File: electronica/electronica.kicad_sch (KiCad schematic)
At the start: 19 parts, among them J1 Arduino_Power, J10 Pump_4, J2 ESP12_Power, J3 Arduino_Serial, J4 DC 5v, J5 ESP12_Serial, J6 Arduino_D8_D11, J7 Pump_1, J8 Pump_2, J9 Pump_3, U1 ULN2003

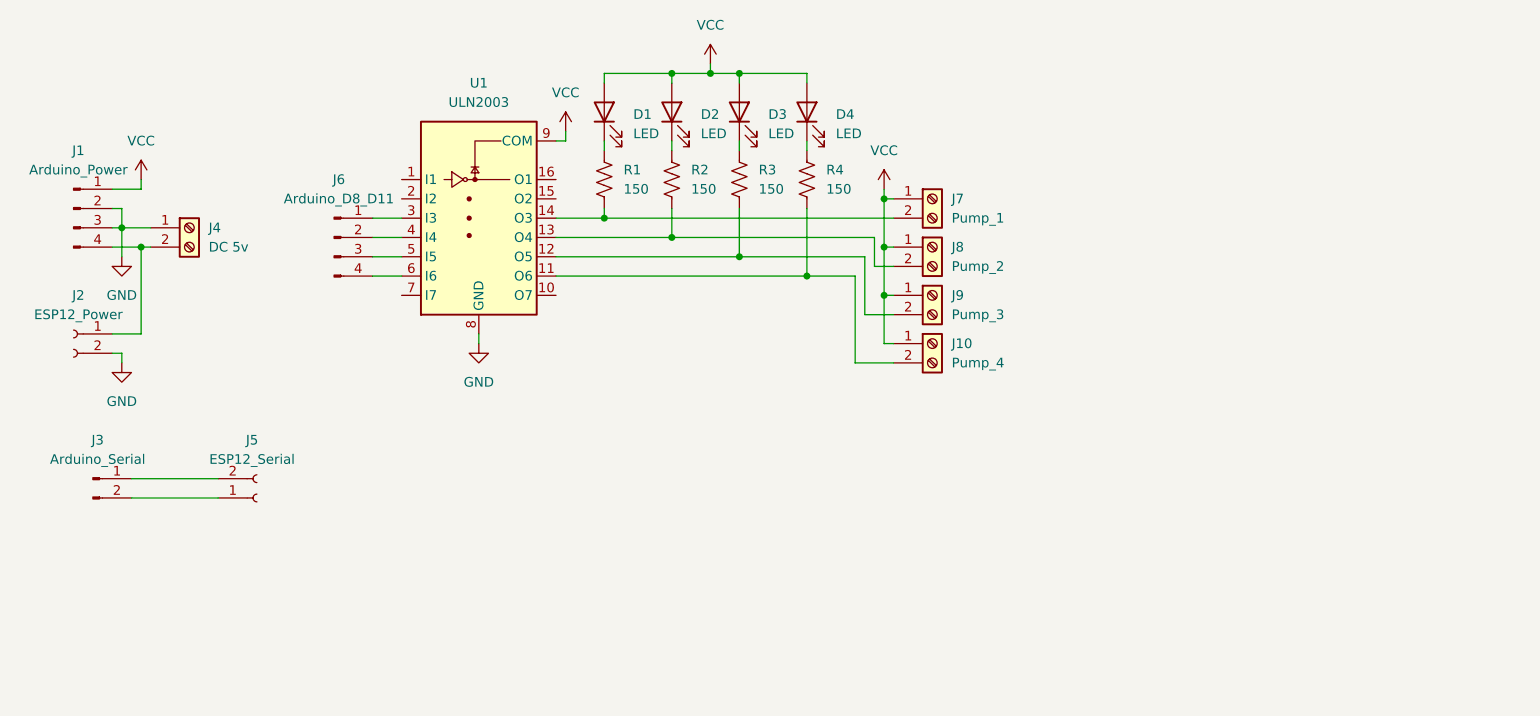
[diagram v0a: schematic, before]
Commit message: Updated schematic and perfboard
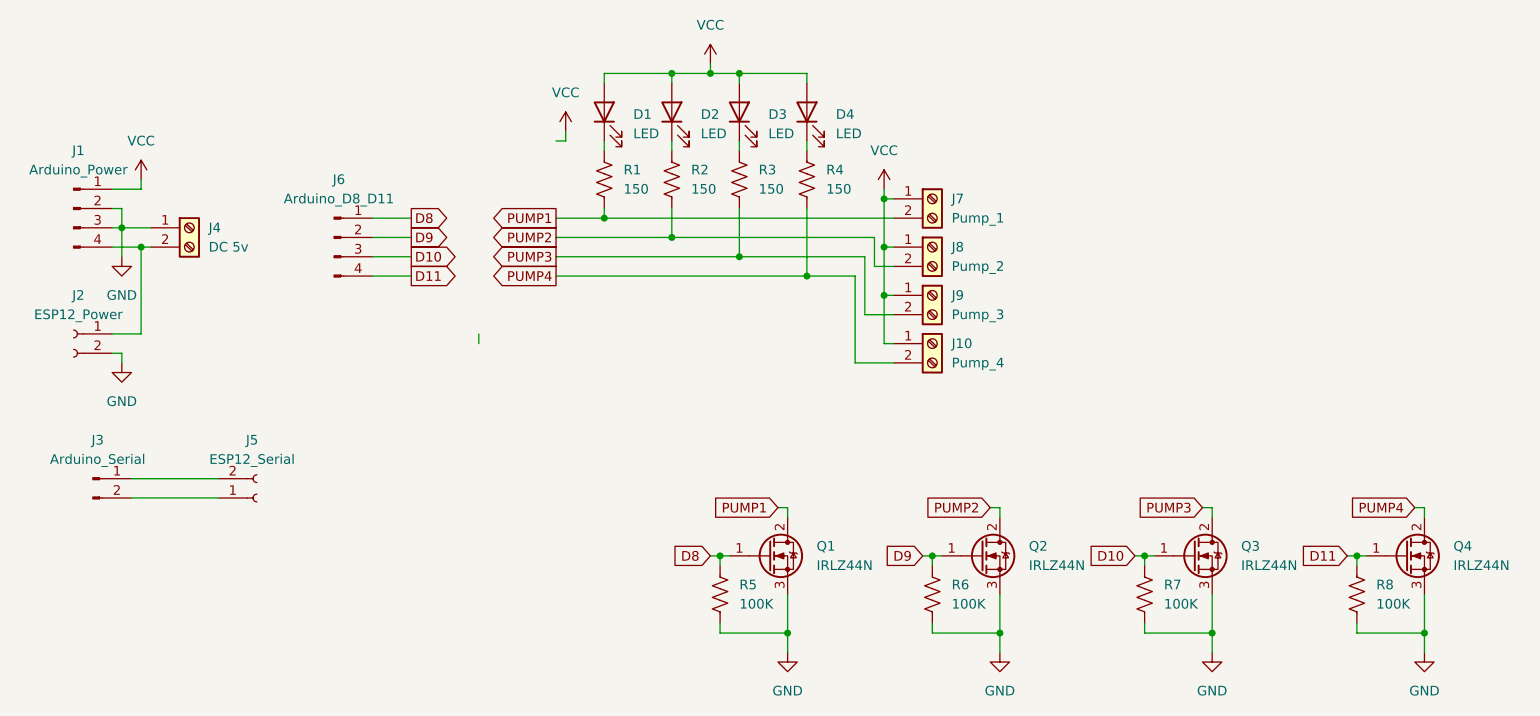
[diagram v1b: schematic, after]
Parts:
- removed U1: ULN2003, symbol Transistor_Array:ULN2003
- added Q1, Q2, Q3, Q4: IRLZ44N, Package_TO_SOT_THT:TO-220-3_Vertical, symbol Transistor_FET:IRLZ44N
- added R5, R6, R7, R8: 100K, symbol Device:R_US
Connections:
- net GND: now also Q1.3 (S), Q2.3 (S), Q3.3 (S), Q4.3 (S), R5.2, R6.2, R7.2, R8.2
- net PUMP2: now reaches J8.2 (Pin_2), R2.2
- net PUMP2: now also Q2.2 (D)
- net PUMP3: now reaches J9.2 (Pin_2), R3.2
- net PUMP3: now also Q3.2 (D)
- net PUMP1: now reaches J7.2 (Pin_2), R1.2
- net PUMP1: now also Q1.2 (D)
- net PUMP4: now reaches J10.2 (Pin_2), R4.2
- net PUMP4: now also Q4.2 (D)
- net D8: now reaches J6.1 (Pin_1)
- net D8: now also Q1.1 (G), R5.1
- net D9: now reaches J6.2 (Pin_2)
- net D9: now also Q2.1 (G), R6.1
- net D10: now reaches J6.3 (Pin_3)
- net D10: now also Q3.1 (G), R7.1
- net D11: now reaches J6.4 (Pin_4)
- net D11: now also Q4.1 (G), R8.1
